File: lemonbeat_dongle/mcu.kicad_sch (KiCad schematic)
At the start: 39 parts, among them J201 USB_A, J202 Prog, J203 u.FL, SW201 SW_Push, U201 nRF52840, Y201 32MHz, Y202 32.768kHz

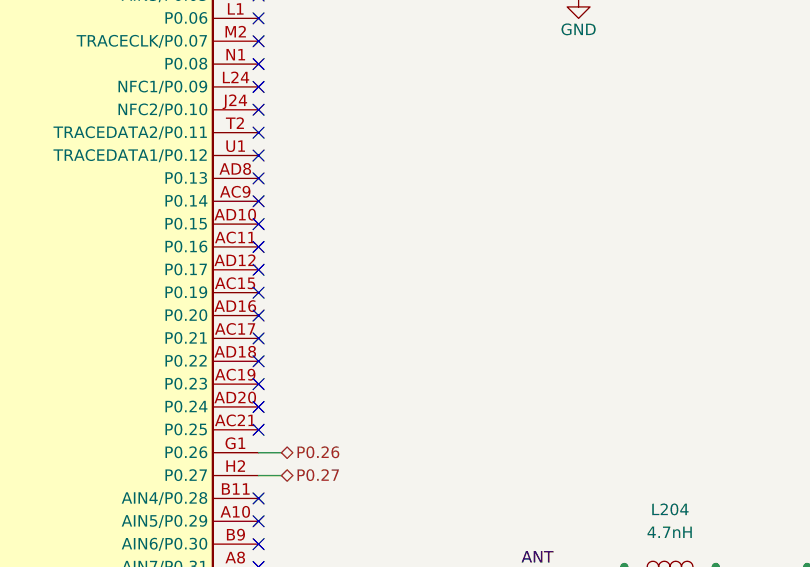
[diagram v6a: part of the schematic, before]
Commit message: dongle: connect RESET to P0.17
This is needed to route the RESET pin (on inner ring) on the PCB.

Note: same trick was used on LCGW with nRF52840.
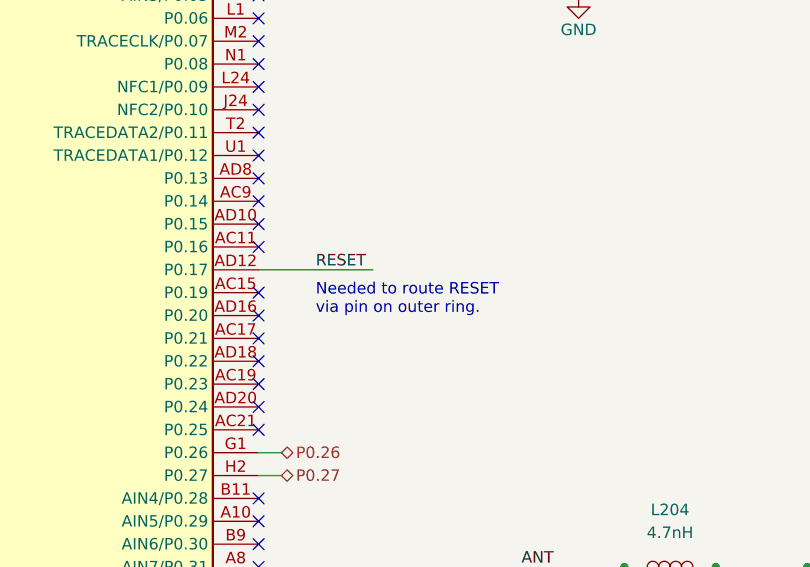
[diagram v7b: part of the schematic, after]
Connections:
- net RESET: now also U201.AD12 (P0.17)
- no-connect marks 40 -> 39
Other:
- note added: "Needed to route RESET via pin on outer ring."
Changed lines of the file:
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@@
   (no_connect (at 121.92 62.23))
   (no_connect (at 121.92 143.51))
-  (no_connect (at 121.92 97.79))
   (no_connect (at 121.92 110.49))
   (no_connect (at 121.92 102.87))
@@
     (stroke (width 0) (type default) (color 0 0 0 0))
   )
+  (wire (pts (xy 121.92 97.79) (xy 134.62 97.79))
+    (stroke (width 0) (type default) (color 0 0 0 0))
+  )
   (wire (pts (xy 237.49 115.57) (xy 241.3 115.57))
     (stroke (width 0) (type default) (color 0 0 0 0))
@@
     (effects (font (size 1.27 1.27)) (justify left bottom))
   )
+  (text "Needed to route RESET\nvia pin on outer ring." (at 128.27 102.87 0)
+    (effects (font (size 1.27 1.27)) (justify left bottom))
+  )
   (label "ANT" (at 49.53 72.39 0)
     (effects (font (size 1.27 1.27)) (justify left bottom))
@@
     (effects (font (size 1.27 1.27)) (justify left bottom))
   )
+  (label "RESET" (at 128.27 97.79 0)
+    (effects (font (size 1.27 1.27)) (justify left bottom))
+  )

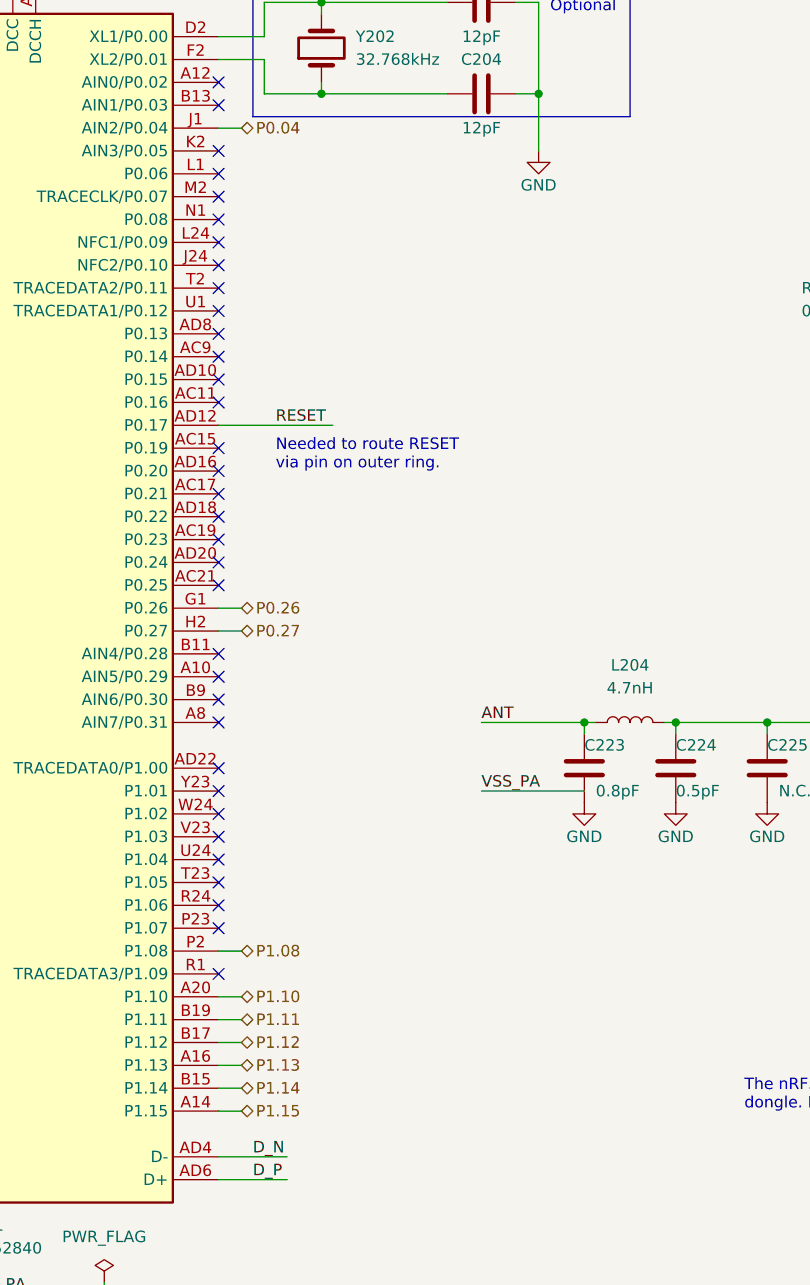
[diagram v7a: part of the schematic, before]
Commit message: dongle: use pins on outer rows of nRF52840
Replace pins on inner row with pins on outer row to facilitate
routing.

All pins for communication with Si4467 are non low-drive pins.
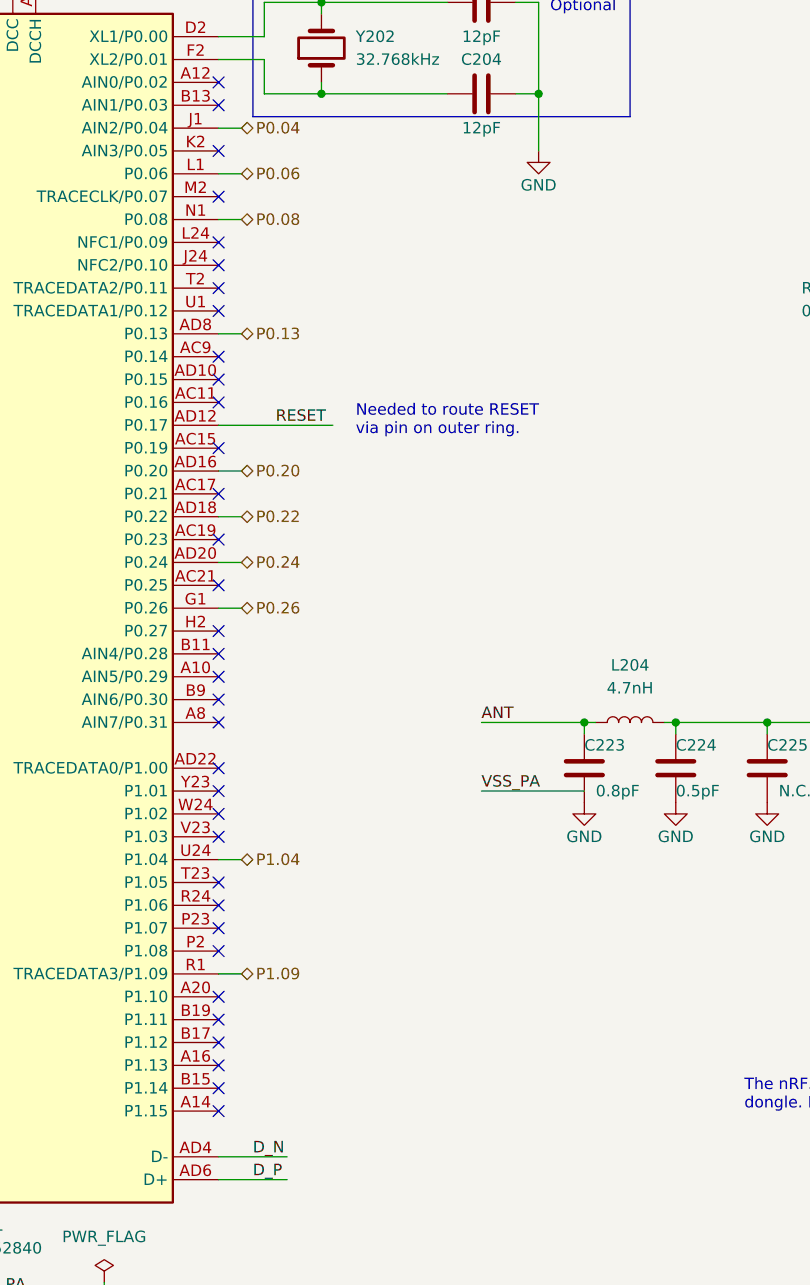
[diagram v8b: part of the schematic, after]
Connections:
- net P0.20: now reaches U201.AD16 (P0.20)
- net P0.22: now reaches U201.AD18 (P0.22)
- net P0.24: now reaches U201.AD20 (P0.24)
- net P0.13: now reaches U201.AD8 (P0.13)
- net P0.06: now reaches U201.L1 (P0.06)
- net P0.08: now reaches U201.N1 (P0.08)
- net P1.09: now reaches U201.R1 (TRACEDATA3/P1.09)
- net P1.04: now reaches U201.U24 (P1.04)
- net P0.27: no longer names the net of U201.H2 (P0.27)
- net P1.08: no longer names the net of U201.P2 (P1.08)
- net P1.10: no longer names the net of U201.A20 (P1.10)
- net P1.11: no longer names the net of U201.B19 (P1.11)
- net P1.12: no longer names the net of U201.B17 (P1.12)
- net P1.13: no longer names the net of U201.A16 (P1.13)
- net P1.14: no longer names the net of U201.B15 (P1.14)
- net P1.15: no longer names the net of U201.A14 (P1.15)
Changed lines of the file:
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@@
   )
   (no_connect (at 121.92 138.43))
-  (no_connect (at 121.92 113.03))
   (no_connect (at 101.6 46.99))
+  (no_connect (at 121.92 72.39))
+  (no_connect (at 121.92 163.83))
   (no_connect (at 121.92 95.25))
   (no_connect (at 121.92 151.13))
   (no_connect (at 121.92 148.59))
+  (no_connect (at 121.92 166.37))
   (no_connect (at 121.92 105.41))
   (no_connect (at 121.92 67.31))
@@
   (no_connect (at 121.92 143.51))
   (no_connect (at 121.92 110.49))
-  (no_connect (at 121.92 102.87))
-  (no_connect (at 121.92 107.95))
+  (no_connect (at 121.92 173.99))
   (no_connect (at 121.92 85.09))
   (no_connect (at 121.92 80.01))
   (no_connect (at 121.92 77.47))
   (no_connect (at 121.92 82.55))
-  (no_connect (at 121.92 87.63))
-  (no_connect (at 121.92 74.93))
-  (no_connect (at 121.92 72.39))
-  (no_connect (at 121.92 69.85))
+  (no_connect (at 121.92 156.21))
+  (no_connect (at 121.92 161.29))
   (no_connect (at 121.92 115.57))
-  (no_connect (at 121.92 158.75))
   (no_connect (at 121.92 153.67))
   (no_connect (at 254 113.03))
@@
   (no_connect (at 241.3 113.03))
   (no_connect (at 121.92 135.89))
-  (no_connect (at 121.92 146.05))
+  (no_connect (at 121.92 171.45))
   (no_connect (at 99.06 46.99))
   (no_connect (at 121.92 140.97))
@@
   (no_connect (at 121.92 130.81))
   (no_connect (at 121.92 128.27))
+  (no_connect (at 121.92 120.65))
   (no_connect (at 121.92 125.73))
   (no_connect (at 121.92 100.33))
+  (no_connect (at 121.92 168.91))
   (wire (pts (xy 157.48 60.96) (xy 157.48 67.31))
     (stroke (width 0) (type default) (color 0 0 0 0))
@@
     (stroke (width 0) (type default) (color 0 0 0 0))
   )
+  (wire (pts (xy 121.92 87.63) (xy 124.46 87.63))
+    (stroke (width 0) (type default) (color 0 0 0 0))
+  )
   (wire (pts (xy 208.28 64.77) (xy 222.25 64.77))
     (stroke (width 0) (type default) (color 0 0 0 0))
@@
     (stroke (width 0) (type default) (color 0 0 0 0))
   )
-  (wire (pts (xy 121.92 120.65) (xy 124.46 120.65))
-    (stroke (width 0) (type default) (color 0 0 0 0))
-  )
   (polyline (pts (xy 58.42 25.4) (xy 58.42 55.88))
     (stroke (width 0) (type default) (color 0 0 0 0))
   )
-  (wire (pts (xy 121.92 173.99) (xy 124.46 173.99))
-    (stroke (width 0) (type default) (color 0 0 0 0))
-  )
   (wire (pts (xy 71.12 39.37) (xy 71.12 46.99))
     (stroke (width 0) (type default) (color 0 0 0 0))
@@
     (stroke (width 0) (type default) (color 0 0 0 0))
   )
-  (wire (pts (xy 121.92 168.91) (xy 124.46 168.91))
-    (stroke (width 0) (type default) (color 0 0 0 0))
-  )
   (wire (pts (xy 121.92 179.07) (xy 129.54 179.07))
     (stroke (width 0) (type default) (color 0 0 0 0))
@@
     (stroke (width 0) (type default) (color 0 0 0 0))
   )
+  (wire (pts (xy 121.92 74.93) (xy 124.46 74.93))
+    (stroke (width 0) (type default) (color 0 0 0 0))
+  )
   (wire (pts (xy 241.3 110.49) (xy 237.49 110.49))
     (stroke (width 0) (type default) (color 0 0 0 0))
   )
-  (wire (pts (xy 121.92 161.29) (xy 124.46 161.29))
-    (stroke (width 0) (type default) (color 0 0 0 0))
-  )
   (wire (pts (xy 49.53 33.02) (xy 49.53 40.64))
     (stroke (width 0) (type default) (color 0 0 0 0))
@@
     (stroke (width 0) (type default) (color 0 0 0 0))
   )
+  (wire (pts (xy 121.92 102.87) (xy 124.46 102.87))
+    (stroke (width 0) (type default) (color 0 0 0 0))
+  )
   (wire (pts (xy 222.25 64.77) (xy 222.25 77.47))
     (stroke (width 0) (type default) (color 0 0 0 0))
   )
+  (wire (pts (xy 121.92 113.03) (xy 124.46 113.03))
+    (stroke (width 0) (type default) (color 0 0 0 0))
+  )
   (wire (pts (xy 259.08 68.58) (xy 259.08 76.2))
     (stroke (width 0) (type default) (color 0 0 0 0))
@@
     (stroke (width 0) (type default) (color 0 0 0 0))
   )
+  (wire (pts (xy 121.92 107.95) (xy 124.46 107.95))
+    (stroke (width 0) (type default) (color 0 0 0 0))
+  )
   (wire (pts (xy 25.4 33.02) (xy 25.4 40.64))
     (stroke (width 0) (type default) (color 0 0 0 0))
@@
     (stroke (width 0) (type default) (color 0 0 0 0))
   )
+  (wire (pts (xy 121.92 69.85) (xy 124.46 69.85))
+    (stroke (width 0) (type default) (color 0 0 0 0))
+  )
   (wire (pts (xy 93.98 46.99) (xy 93.98 43.18))
     (stroke (width 0) (type default) (color 0 0 0 0))
@@
     (stroke (width 0) (type default) (color 0 0 0 0))
   )
-  (wire (pts (xy 121.92 156.21) (xy 124.46 156.21))
-    (stroke (width 0) (type default) (color 0 0 0 0))
-  )
   (wire (pts (xy 27.94 62.23) (xy 27.94 63.5))
     (stroke (width 0) (type default) (color 0 0 0 0))
@@
     (stroke (width 0) (type default) (color 0 0 0 0))
   )
-  (wire (pts (xy 121.92 163.83) (xy 124.46 163.83))
-    (stroke (width 0) (type default) (color 0 0 0 0))
-  )
   (wire (pts (xy 133.35 60.96) (xy 147.32 60.96))
     (stroke (width 0) (type default) (color 0 0 0 0))
@@
     (stroke (width 0) (type default) (color 0 0 0 0))
   )
+  (wire (pts (xy 121.92 146.05) (xy 124.46 146.05))
+    (stroke (width 0) (type default) (color 0 0 0 0))
+  )
   (wire (pts (xy 124.46 19.05) (xy 124.46 20.32))
     (stroke (width 0) (type default) (color 0 0 0 0))
@@
     (stroke (width 0) (type default) (color 0 0 0 0))
   )
-  (wire (pts (xy 121.92 171.45) (xy 124.46 171.45))
-    (stroke (width 0) (type default) (color 0 0 0 0))
-  )
   (wire (pts (xy 73.66 21.59) (xy 91.44 21.59))
     (stroke (width 0) (type default) (color 0 0 0 0))
@@
     (stroke (width 0) (type default) (color 0 0 0 0))
   )
+  (wire (pts (xy 121.92 158.75) (xy 124.46 158.75))
+    (stroke (width 0) (type default) (color 0 0 0 0))
+  )
   (wire (pts (xy 91.44 194.31) (xy 109.22 194.31))
     (stroke (width 0) (type default) (color 0 0 0 0))
@@
   )
   (wire (pts (xy 237.49 105.41) (xy 241.3 105.41))
-    (stroke (width 0) (type default) (color 0 0 0 0))
-  )
-  (wire (pts (xy 121.92 166.37) (xy 124.46 166.37))
     (stroke (width 0) (type default) (color 0 0 0 0))
   )
@@
     (effects (font (size 1.27 1.27)) (justify left bottom))
   )
-  (text "Needed to route RESET\nvia pin on outer ring." (at 128.27 102.87 0)
+  (text "Needed to route RESET\nvia pin on outer ring." (at 137.16 99.06 0)
     (effects (font (size 1.27 1.27)) (justify left bottom))
   )
@@
     (effects (font (size 1.27 1.27)) (justify left bottom))
   )
-  (hierarchical_label "P1.08" (shape bidirectional) (at 124.46 156.21 0)
+  (hierarchical_label "P1.09" (shape bidirectional) (at 124.46 158.75 0)
+    (effects (font (size 1.27 1.27)) (justify left))
+  )
+  (hierarchical_label "P1.04" (shape bidirectional) (at 124.46 146.05 0)
     (effects (font (size 1.27 1.27)) (justify left))
   )
@@
     (effects (font (size 1.27 1.27)) (justify left))
   )
-  (hierarchical_label "P1.13" (shape bidirectional) (at 124.46 168.91 0)
-    (effects (font (size 1.27 1.27)) (justify left))
-  )
-  (hierarchical_label "P1.15" (shape bidirectional) (at 124.46 173.99 0)
-    (effects (font (size 1.27 1.27)) (justify left))
-  )
-  (hierarchical_label "P1.14" (shape bidirectional) (at 124.46 171.45 0)
-    (effects (font (size 1.27 1.27)) (justify left))
-  )
-  (hierarchical_label "P1.11" (shape bidirectional) (at 124.46 163.83 0)
+  (hierarchical_label "P0.13" (shape bidirectional) (at 124.46 87.63 0)
+    (effects (font (size 1.27 1.27)) (justify left))
+  )
+  (hierarchical_label "P0.08" (shape bidirectional) (at 124.46 74.93 0)
+    (effects (font (size 1.27 1.27)) (justify left))
+  )
+  (hierarchical_label "P0.22" (shape bidirectional) (at 124.46 107.95 0)
+    (effects (font (size 1.27 1.27)) (justify left))
+  )
+  (hierarchical_label "P0.20" (shape bidirectional) (at 124.46 102.87 0)
     (effects (font (size 1.27 1.27)) (justify left))
   )
@@
     (effects (font (size 1.27 1.27)) (justify left))
   )
-  (hierarchical_label "P1.10" (shape bidirectional) (at 124.46 161.29 0)
-    (effects (font (size 1.27 1.27)) (justify left))
-  )
-  (hierarchical_label "P0.27" (shape bidirectional) (at 124.46 120.65 0)
-    (effects (font (size 1.27 1.27)) (justify left))
-  )
-  (hierarchical_label "P1.12" (shape bidirectional) (at 124.46 166.37 0)
-    (effects (font (size 1.27 1.27)) (justify left))
-  )
+  (hierarchical_label "P0.06" (shape bidirectional) (at 124.46 69.85 0)
+    (effects (font (size 1.27 1.27)) (justify left))
+  )
+  (hierarchical_label "P0.24" (shape bidirectional) (at 124.46 113.03 0)
+    (effects (font (size 1.27 1.27)) (justify left))
+  )
